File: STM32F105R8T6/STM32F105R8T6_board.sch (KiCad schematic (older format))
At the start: 22 parts, among them J2 DC_POWER_JACK, SW1 SW_PUSH, U1 STM32F105R8T6, X1 CRYSTAL, X2 CRYSTAL

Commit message: Some changes here
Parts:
- gave numbers to parts that had none: 1
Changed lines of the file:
@@
-EESchema Schematic File Version 2  date dom 10 abr 2011 19:25:27 ART
+EESchema Schematic File Version 2  date dom 10 abr 2011 19:52:04 ART
 LIBS:power
 LIBS:device
@@
 Connection ~ 8550 14050
 $Comp
-L +3.3V #PWR?
+L +3.3V #PWR01
 U 1 1 4DA22E4D
 P 10050 13350
-F 0 "#PWR?" H 10050 13310 30  0001 C CNN
+F 0 "#PWR01" H 10050 13310 30  0001 C CNN
 F 1 "+3.3V" H 10050 13460 30  0000 C CNN
 	1    10050 13350
@@
 $EndComp
 $Comp
-L GND #PWR?
+L GND #PWR02
 U 1 1 4DA22D8E
 P 9100 14200
-F 0 "#PWR?" H 9100 14200 30  0001 C CNN
+F 0 "#PWR02" H 9100 14200 30  0001 C CNN
 F 1 "GND" H 9100 14130 30  0001 C CNN
 	1    9100 14200
@@
 $EndComp
 $Comp
-L 1117 U?
+L 1117 U2
 U 1 1 4DA22D7B
 P 9100 13500
-F 0 "U?" H 9250 13304 50  0000 C CNN
+F 0 "U2" H 9250 13304 50  0000 C CNN
 F 1 "1117" H 9100 13650 40  0000 C CNN
 	1    9100 13500
@@
 $EndComp
 $Comp
-L GND #PWR01
+L GND #PWR03
 U 1 1 4DA2007D
 P 9450 10000
-F 0 "#PWR01" H 9450 10000 30  0001 C CNN
+F 0 "#PWR03" H 9450 10000 30  0001 C CNN
 F 1 "GND" H 9450 9930 30  0001 C CNN
 	1    9450 10000
@@
 $EndComp
 $Comp
-L +3.3V #PWR02
+L +3.3V #PWR04
 U 1 1 4DA2003E
 P 10450 9300
-F 0 "#PWR02" H 10450 9260 30  0001 C CNN
+F 0 "#PWR04" H 10450 9260 30  0001 C CNN
 F 1 "+3.3V" H 10450 9410 30  0000 C CNN
 	1    10450 9300
@@
 $EndComp
 $Comp
-L GND #PWR03
+L GND #PWR05
 U 1 1 4DA1F7EC
 P 9300 7450
-F 0 "#PWR03" H 9300 7450 30  0001 C CNN
+F 0 "#PWR05" H 9300 7450 30  0001 C CNN
 F 1 "GND" H 9300 7380 30  0001 C CNN
 	1    9300 7450
@@
 $EndComp
 $Comp
-L GND #PWR04
+L GND #PWR06
 U 1 1 4DA1F7E8
 P 9300 5650
-F 0 "#PWR04" H 9300 5650 30  0001 C CNN
+F 0 "#PWR06" H 9300 5650 30  0001 C CNN
 F 1 "GND" H 9300 5580 30  0001 C CNN
 	1    9300 5650
@@
 NRST
 $Comp
-L GND #PWR05
+L GND #PWR07
 U 1 1 4DA13FF8
 P 11200 13900
-F 0 "#PWR05" H 11200 13900 30  0001 C CNN
+F 0 "#PWR07" H 11200 13900 30  0001 C CNN
 F 1 "GND" H 11200 13830 30  0001 C CNN
 	1    11200 13900
@@
 $EndComp
 $Comp
-L GND #PWR06
+L GND #PWR08
 U 1 1 4DA13F94
 P 10650 6100
-F 0 "#PWR06" H 10650 6100 30  0001 C CNN
+F 0 "#PWR08" H 10650 6100 30  0001 C CNN
 F 1 "GND" H 10650 6030 30  0001 C CNN
 	1    10650 6100
@@
 $EndComp
 $Comp
-L GND #PWR07
+L GND #PWR09
 U 1 1 4DA13F8F
 P 10650 7250
-F 0 "#PWR07" H 10650 7250 30  0001 C CNN
+F 0 "#PWR09" H 10650 7250 30  0001 C CNN
 F 1 "GND" H 10650 7180 30  0001 C CNN
 	1    10650 7250
@@
 $EndComp
 $Comp
-L GND #PWR08
+L GND #PWR010
 U 1 1 4DA13F88
 P 10650 8000
-F 0 "#PWR08" H 10650 8000 30  0001 C CNN
+F 0 "#PWR010" H 10650 8000 30  0001 C CNN
 F 1 "GND" H 10650 7930 30  0001 C CNN
 	1    10650 8000
@@
 $EndComp
 $Comp
-L GND #PWR09
+L GND #PWR011
 U 1 1 4DA13F84
 P 10600 9300
-F 0 "#PWR09" H 10600 9300 30  0001 C CNN
+F 0 "#PWR011" H 10600 9300 30  0001 C CNN
 F 1 "GND" H 10600 9230 30  0001 C CNN
 	1    10600 9300
@@
 $EndComp
 $Comp
-L GND #PWR010
+L GND #PWR012
 U 1 1 4DA13F77
 P 10900 11350
-F 0 "#PWR010" H 10900 11350 30  0001 C CNN
+F 0 "#PWR012" H 10900 11350 30  0001 C CNN
 F 1 "GND" H 10900 11280 30  0001 C CNN
 	1    10900 11350
@@
 $EndComp
 $Comp
-L GND #PWR011
+L GND #PWR013
 U 1 1 4DA13F71
 P 10900 9600
-F 0 "#PWR011" H 10900 9600 30  0001 C CNN
+F 0 "#PWR013" H 10900 9600 30  0001 C CNN
 F 1 "GND" H 10900 9530 30  0001 C CNN
 	1    10900 9600
@@
 $EndComp
 $Comp
-L +3.3V #PWR012
+L +3.3V #PWR014
 U 1 1 4DA13F5F
 P 11550 5700
-F 0 "#PWR012" H 11550 5660 30  0001 C CNN
+F 0 "#PWR014" H 11550 5660 30  0001 C CNN
 F 1 "+3.3V" H 11550 5810 30  0000 C CNN
 	1    11550 5700

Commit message: Algo de limpieza. Esquematico al 90% y primer ruteo
Signed-off-by: Martin Ribelotta <martinribelotta@gmail.com>
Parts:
- added JTAG1: CONN_4X2, symbol CONN_4X2
- added PIO1, PIO2: CONN_10X2, symbol CONN_10X2
- added R2, R3, R4, R5, R6, R7, R8: R, symbol R
- added USB_DEV1: USB_1, symbol USB_1
- added USB_HOST1: USB_2, symbol USB_2
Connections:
- net +3.3V: now also JTAG1.1, PIO1.20 (P20)
- net GND: now also JTAG1.2, JTAG1.8, PIO2.1 (P1), R4.1, R7.2, R8.2, USB_DEV1.4 (GND), USB_HOST1.4
- net JTCK/SWCLK: now also JTAG1.3
- net JTDI: now also JTAG1.5
- net JTDO/TRACESWO: now also JTAG1.4
- net JTMS/SWDIO: now also JTAG1.6
- net NJTRST: now also JTAG1.7
- net NRST: now also PIO2.4 (P4)
- net PC2: now reaches U1.10 (PC2/ADC12_IN12/ETH_MII_TXD2)
- net PC2: now also PIO1.3 (P3)
- net PC3: now reaches U1.11 (PC3/ADC12_IN13/ETH_MII_TX_CLK)
- net PC3: now also PIO1.4 (P4)
- net PA0: now reaches U1.14 (PA0/USART2_CTS/ADC12_IN0/TIM2_CH1_ETR/TIM5_CH1/ETH_MII_CRS_WKUP)
- net PA0: now also PIO1.5 (P5)
- net PA1: now reaches U1.15 (PA1/USART2_RTS/ADC12_IN1/TIM5_CH2/TIM2_CH2/ETH_MII_RX_CLK/ETH_RMII_REF_CLK)
- net PA1: now also PIO1.6 (P6)
- net PA2: now reaches U1.16 (PA2/USART2_TX/TIM5_CH3/ADC12_IN2/TIM2_CH3/ETH_MII_MDIO/ETH_RMII_MDIO)
- net PA2: now also PIO1.7 (P7)
- net PA3: now reaches U1.17 (PA3/USART2_RX/TIM5_CH4/ADC12_IN3/TIM2_CH4/ETH_MII_COL)
- net PA3: now also PIO1.8 (P8)
- net PC13: now reaches U1.2 (PC13-TAMPER-RTC)
- net PC13: now also PIO2.2 (P2)
- net PA4: now reaches U1.20 (PA4/SPI1_NSS/DAC_OUT1/USART2_CK/ADC12_IN4)
- net PA4: now also PIO1.9 (P9)
- net PA5: now reaches U1.21 (PA5/SPI1_SCK/DAC_OUT2/ADC12_IN5)
- net PA5: now also PIO1.10 (P10)
- net PA6: now reaches U1.22 (PA6/SPI1_MISO/ADC12_IN6/TIM3_CH1)
- net PA6: now also PIO1.11 (P11)
- net PA7: now reaches U1.23 (PA7/SPI1_MOSI/ADC12_IN7/TIM3_CH2/ETH_MII_RX_DV/ETH_RMII_CRS_DV)
- net PA7: now also PIO1.12 (P12)
- net PC4: now reaches U1.24 (PC4/ADC12_IN14/ETH_MII_RXD0/ETH_RMII_RXD0)
- net PC4: now also PIO1.13 (P13)
- net PC5: now reaches U1.25 (PC5/ADC12_IN15/ETH_MII_RXD1/ETH_RMII_RXD1)
- net PC5: now also PIO1.14 (P14)
- net PB0: now reaches U1.26 (PB0/ADC12_IN8/TIM3_CH3/ETH_MII_RXD2)
- net PB0: now also PIO1.15 (P15)
- net PB1: now reaches U1.27 (PB1/ADC12_IN9/TIM3_CH4/ETH_MII_RXD3)
- net PB1: now also PIO1.16 (P16)
- net PB2: now reaches U1.28 (PB2/BOOT1)
- net PB2: now also PIO1.17 (P17)
- net PB10: now reaches U1.29 (PB10/I2C2_SCL/USART3_TX/ETH_MII_RX_ER)
- net PB10: now also PIO1.18 (P18)
- net PB11: now reaches U1.30 (PB11/I2C2_SDA/USART3_RX/ETH_MII_TX_EN/ETH_RMII_TX_EN)
- net PB11: now also PIO1.19 (P19)
- net PB12: now reaches U1.33 (PB12/SPI2_NSS/I2S2_WS/I2C2_SMBA/USART3_CK/TIM1_BKIN/CAN2_RX/ETH_MII_TXD0/ETH_RMII_TXD0)
- net PB12: now also PIO2.14 (P14)
- net PB13: now reaches U1.34 (PB13/SPI2_SCK/I2S2_CK/USART3_CTS/TIM1_CH1N/CAN2_TX/ETH_MII_TXD1/ETH_RMII_TXD1)
- net PB13: now also PIO2.13 (P13)
- net PB14: now reaches U1.35 (PB14/SPI2_MISO/TIM1_CH2N/USART3_RTS)
- net PB14: now also PIO2.16 (P16)
- net PB15: now reaches U1.36 (PB15/SPI2_MOSI/I2S2_SD/TIM1_CH3N)
- net PB15: now also PIO2.15 (P15)
- net PC6: now reaches U1.37 (PC6/I2S2_MCK)
- net PC6: now also PIO2.18 (P18)
- net PC7: now reaches U1.38 (PC7/I2S3_MCK)
- net PC7: now also PIO2.17 (P17)
- net PC8: now reaches U1.39 (PC8)
- net PC8: now also PIO2.20 (P20)
- net PC9: now reaches U1.40 (PC9)
- net PC9: now also PIO2.19 (P19)
- net OTG_FS_SOF: now reaches U1.41 (PA8/USART1_CK/OTG_FS_SOF/TIM1_CH1/MCO)
- net OTG_FS_SOF: now also R6.2, R8.1
- net OTG_FS_VBUS: now reaches U1.42 (PA9/USART1_TX/TIM1_CH2/OTG_FS_VBUS)
- net OTG_FS_VBUS: now also R5.2, R7.1
- net OTG_FS_ID: now reaches U1.43 (PA10/USART1_RX/TIM1_CH3/OTG_FS_ID)
- net OTG_FS_ID: now also R4.2
- net OTG_FS_DM: now reaches U1.44 (PA11/USART1_CTS/CAN1_RX/TIM1_CH4/OTG_FS_DM)
- net OTG_FS_DM: now also R3.2
- net OTG_FS_DP: now reaches U1.45 (PA12/USART1_RTS/OTG_FS_DP/CAN1_TX/TIM1_ETR)
- net OTG_FS_DP: now also R2.2
- net PC10: now reaches U1.51 (PC10/UART4_TX)
- net PC10: now also PIO2.11 (P11)
- net PC11: now reaches U1.52 (PC11/UART4_RX)
- net PC11: now also PIO2.12 (P12)
- net PC12: now reaches U1.53 (PC12/UART5_TX)
- net PC12: now also PIO2.9 (P9)
- net PD2: now reaches U1.54 (PD2/TIM3_ETR/UART5_RX)
- net PD2: now also PIO2.10 (P10)
- net PB5: now reaches U1.57 (PB5/I2C1_SMBA/SPI3_MOSI/ETH_MII_PPS_OUT/I2S3_SD/ETH_RMII_PPS_OUT)
- net PB5: now also PIO2.7 (P7)
- net PB6: now reaches U1.58 (PB6/I2C1_SCL/TIM4_CH1)
- net PB6: now also PIO2.8 (P8)
- net PB7: now reaches U1.59 (PB7/I2C1_SDA/TIM4_CH2)
- net PB7: now also PIO2.5 (P5)
- net PB8: now reaches U1.61 (PB8/TIM4_CH3/ETH_MII_TXD3)
- net PB8: now also PIO2.6 (P6)
- net PB9: now reaches U1.62 (PB9/TIM4_CH4)
- net PB9: now also PIO2.3 (P3)
- net PC0: now reaches U1.8 (PC0/ADC12_IN0)
- net PC0: now also PIO1.1 (P1)
- net PC1: now reaches U1.9 (PC1/ADC12_IN11/ETH_MII_MDC/ETH_RMII_MDC)
- net PC1: now also PIO1.2 (P2)
- new net: R2.1, USB_DEV1.3 (D+), USB_HOST1.3
- new net: R3.1, USB_DEV1.2 (D-), USB_HOST1.2
- new net: R5.1, R6.1, USB_DEV1.1 (Vbus), USB_HOST1.1
- no-connect marks 0 -> 2

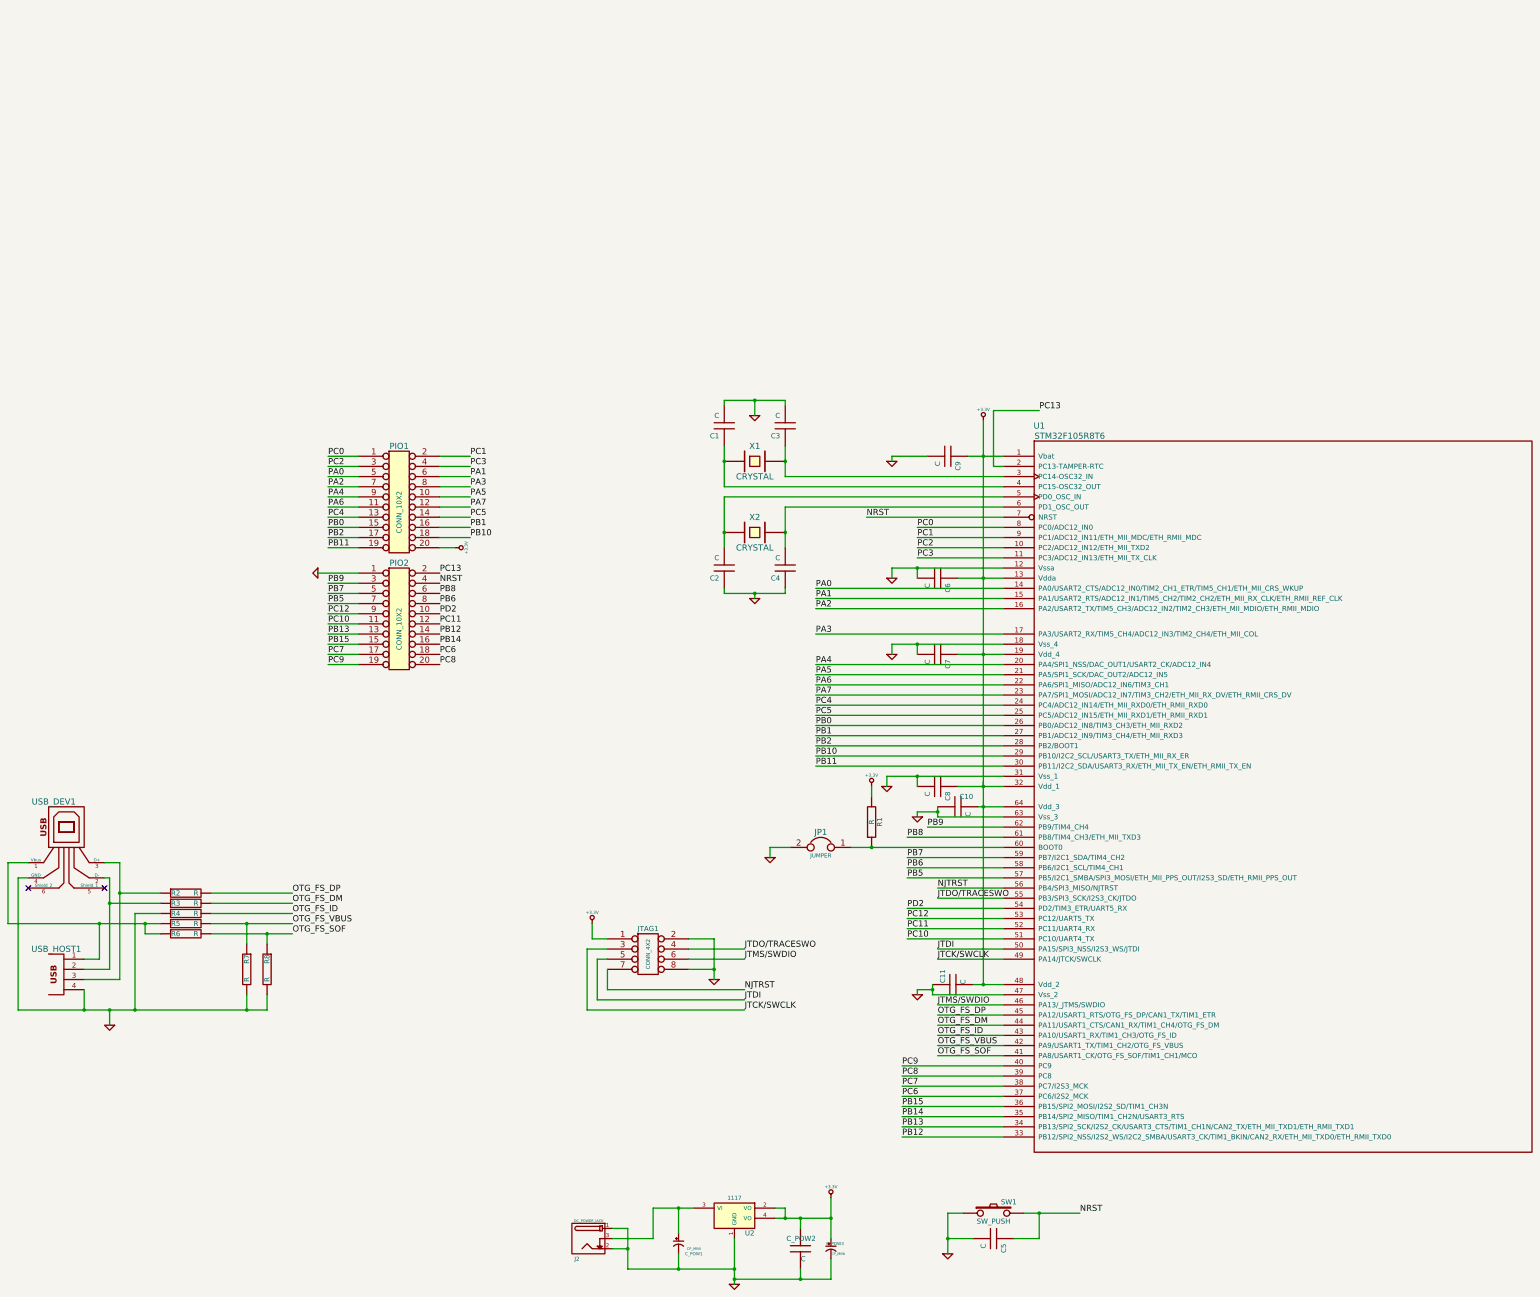
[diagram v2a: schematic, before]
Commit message: Ruteo nuevo para la tarjeta STM32. Modifiaciónes al esquematico.
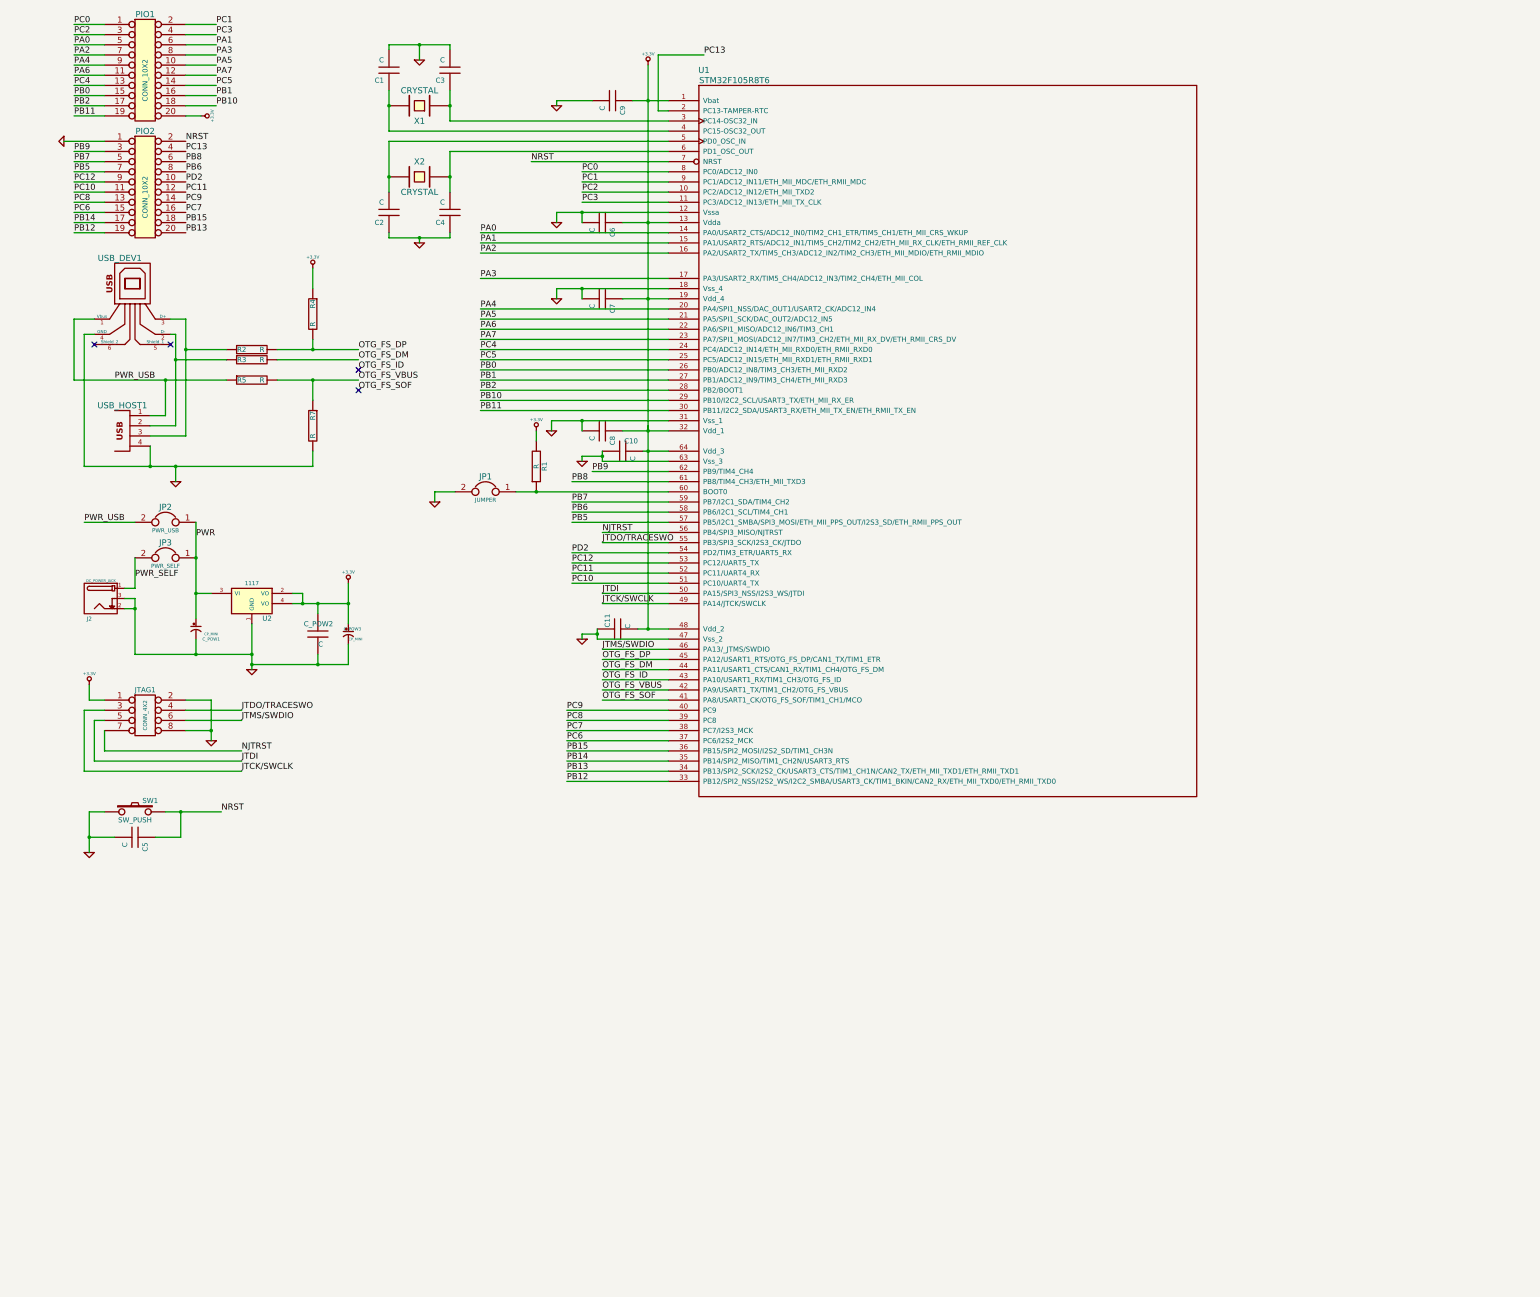
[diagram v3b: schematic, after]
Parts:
- removed R6, R8: R, symbol R
- added JP2: PWR_USB, symbol JUMPER
- added JP3: PWR_SELF, symbol JUMPER
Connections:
- net +3.3V: now also R4.1
- net GND: now also J2.3; no longer J2.1, R4.1
- net NRST: now also PIO2.2 (P2); no longer PIO2.4 (P4)
- net OTG_FS_DP: now also R4.2
- net OTG_FS_ID: no longer R4.2
- net PB12: now also PIO2.19 (P19); no longer PIO2.14 (P14)
- net PB13: now also PIO2.20 (P20); no longer PIO2.13 (P13)
- net PB14: now also PIO2.17 (P17); no longer PIO2.16 (P16)
- net PB15: now also PIO2.18 (P18); no longer PIO2.15 (P15)
- net PC13: now also PIO2.4 (P4); no longer PIO2.2 (P2)
- net PC6: now also PIO2.15 (P15); no longer PIO2.18 (P18)
- net PC7: now also PIO2.16 (P16); no longer PIO2.17 (P17)
- net PC8: now also PIO2.13 (P13); no longer PIO2.20 (P20)
- net PC9: now also PIO2.14 (P14); no longer PIO2.19 (P19)
- net at C1.1, U1.4 (PC15-OSC32_OUT): now also X1.2; no longer X1.1
- net at C3.1, U1.3 (PC14-OSC32_IN): now also X1.1; no longer X1.2
- net PWR: now reaches C_POW1.2, U2.3 (VI)
- net PWR: now also JP2.1, JP3.1; no longer J2.3
- net PWR_USB: now reaches R5.1, USB_DEV1.1 (Vbus), USB_HOST1.1
- net PWR_USB: now also JP2.2
- new net PWR_SELF: J2.1, JP3.2
- no-connect marks 2 -> 4
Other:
- moved on the sheet: C1, C10, C11, C2, C3, C4, C5, C6, C7, C8, C9, C_POW1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
